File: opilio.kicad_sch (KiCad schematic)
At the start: 92 parts, among them J1 SATA_Power_Connector, J2 USB_C_Receptacle_USB2.0, J3 Conn_01x04_Male, J6 Conn_01x06_Male, Q1 CJ3134KW, Q2 AO3401A, Q3 CJ3134KW, Q4 AO3401A, SW1 Reset, SW2 Boot, U1 EUP3458, U2 STM32F103C8T6, U3 USBLC6-2SC6, Y1 TAXM8M4RFDCET2T, Y2 YST310S 32.768KHz

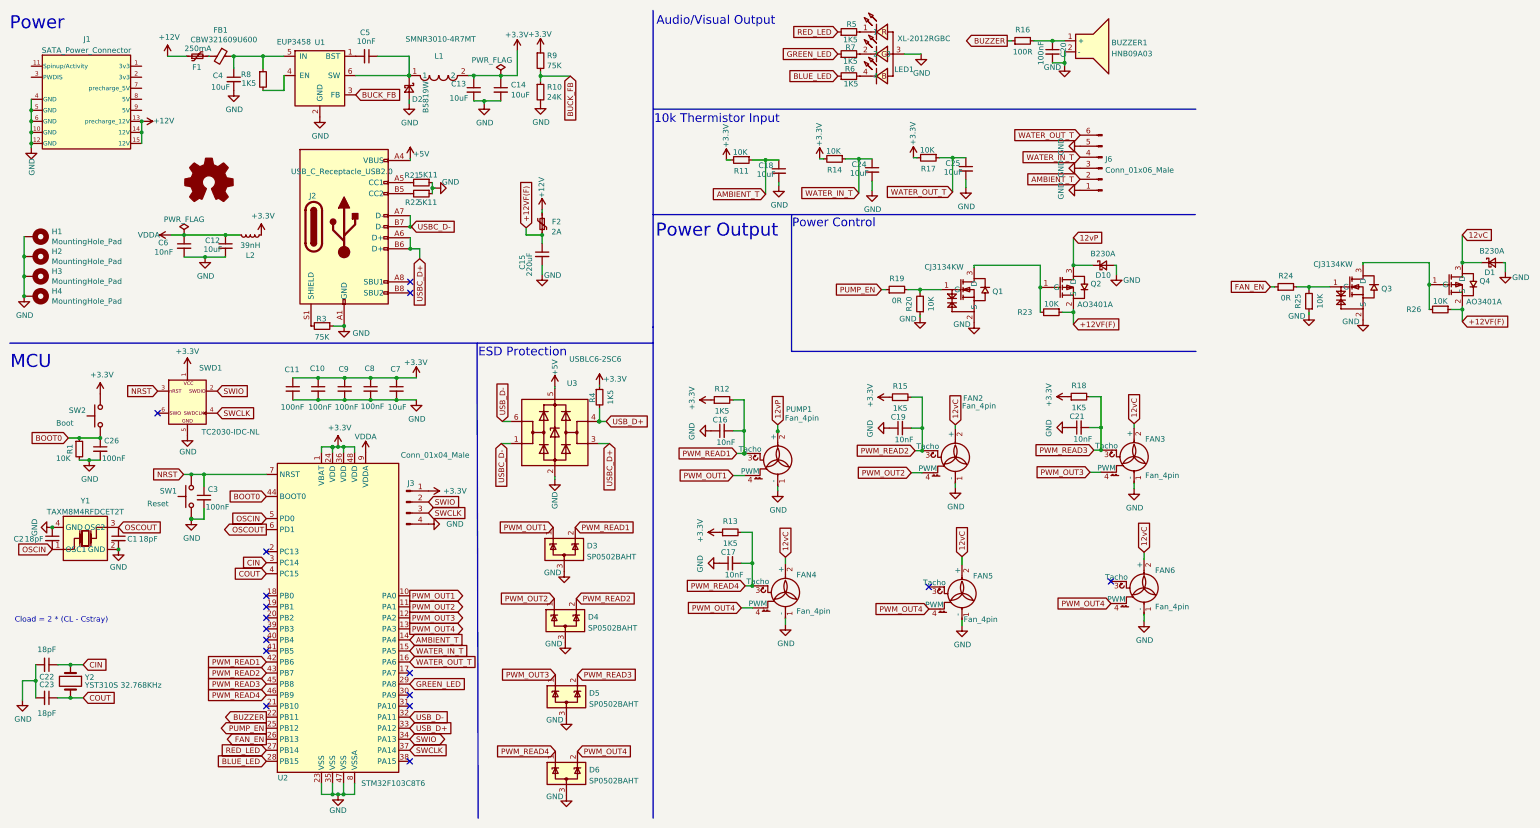
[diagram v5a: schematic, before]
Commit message: split schema, re-route, horizontal fan connectors
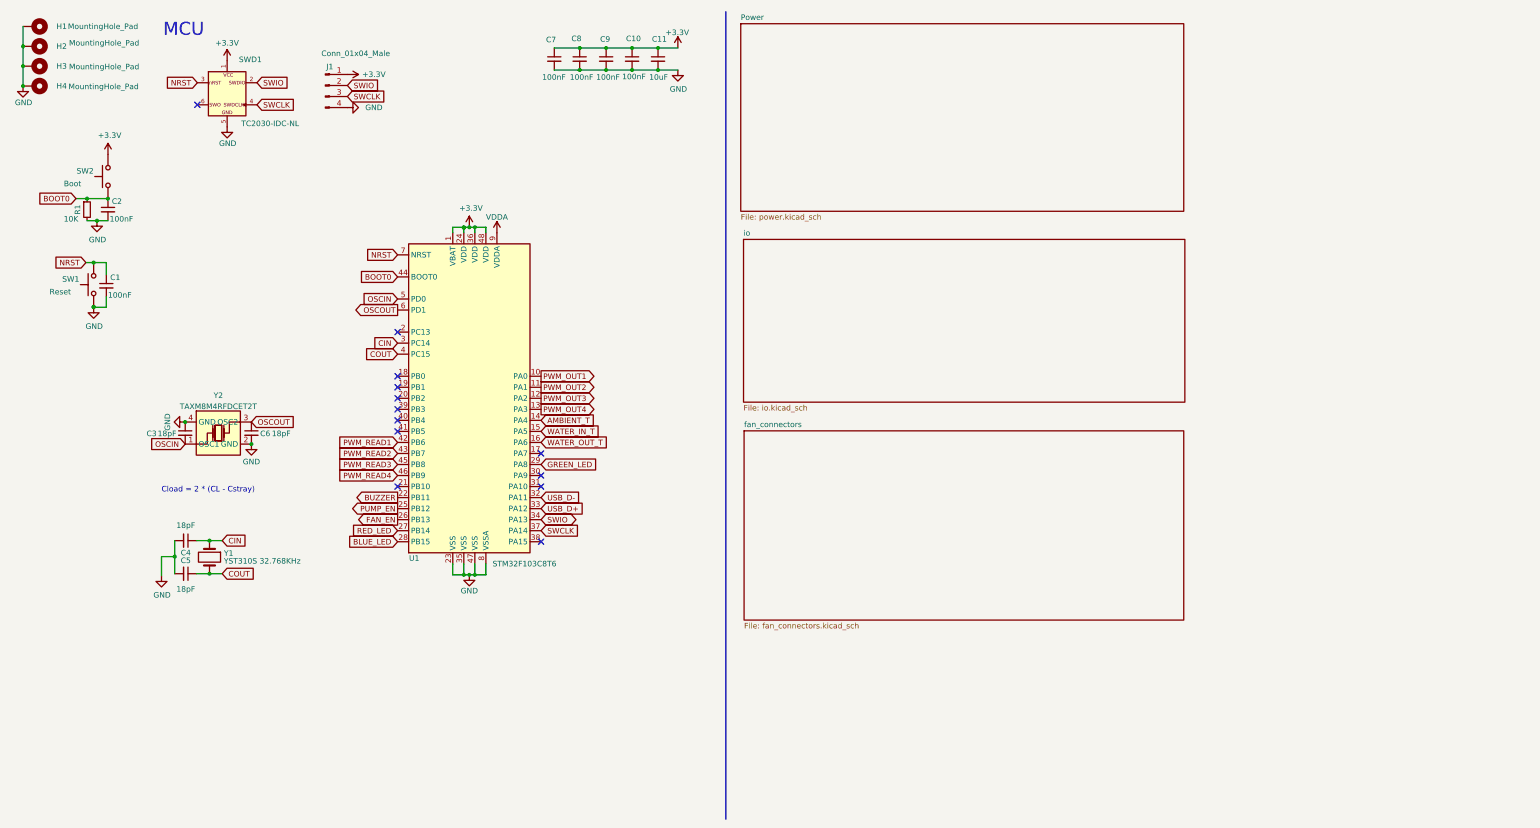
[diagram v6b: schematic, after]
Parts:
- removed BUZZER1: HNB09A03, easyeda2kicad:BUZ-TH_BD9.0-P5.00-D0.6-FD, symbol easyeda:HNB09A03
- removed C12, C13, C14, C18, C24, C25, C4: 10uF, Capacitor_SMD:C_0603_1608Metric, symbol Device:C_Small
- removed C15: 220uF, Capacitor_SMD:CP_Elec_6.3x7.7, symbol Device:C_Small
- removed C16, C17, C19, C21, C5, C6: 10nF, Capacitor_SMD:C_0402_1005Metric, symbol Device:C_Small
- removed C20: 100nF, Capacitor_SMD:C_0402_1005Metric, symbol Device:C_Small
- removed D1, D10: B230A, Diode_SMD:D_SMA, symbol Device:D_Schottky_Small
- removed D2: B5819W, Diode_SMD:D_SOD-123, symbol Device:D_Schottky_Small
- removed D3, D4, D5, D6: SP0502BAHT, Package_TO_SOT_SMD:SOT-23, symbol Power_Protection:SP0502BAHT
- removed F1: 250mA, Fuse:Fuse_1206_3216Metric, symbol Device:Polyfuse_Small
- removed F2: 2A, Fuse:Fuse_1206_3216Metric, symbol Device:Polyfuse_Small
- removed FAN2, FAN3, FAN4, FAN5, FAN6, PUMP1: Fan_4pin, Custom:FanPinHeader_1x04_P2.54mm_Vertical_no_hole, symbol Motor:Fan_4pin
- removed FB1: CBW321609U600, Capacitor_SMD:C_1206_3216Metric, symbol Device:FerriteBead_Small
- removed J1: SATA_Power_Connector, Custom:Sata_Power_Connector_SMD, symbol Custom:SATA_Power_Connector
- removed J2: USB_C_Receptacle_USB2.0, Custom:USB_C_Receptacle_Palconn_UTC16-G_Streached_pads, symbol Connector:USB_C_Receptacle_USB2.0
- removed J6: Conn_01x06_Male, Connector_PinHeader_2.54mm:PinHeader_2x03_P2.54mm_Vertical, symbol Connector:Conn_01x06_Male
- removed L1: SMNR3010-4R7MT, easyeda2kicad:IND-SMD_L3.0-W3.0_SMNR3010, symbol easyeda:SMNR3010-4R7MT
- removed L2: 39nH, Inductor_SMD:L_0805_2012Metric, symbol Device:L_Small
- removed LED1: XL-2012RGBC, easyeda2kicad:LED-SMD_4P-L2.0-W1.3-BR, symbol easyeda:XL-2012RGBC
- removed LOGO1: Logo_Open_Hardware_Small, Symbol:OSHW-Logo2_9.8x8mm_SilkScreen, symbol Graphic:Logo_Open_Hardware_Small
- removed Q1, Q3: CJ3134KW, easyeda2kicad:SC-70-3_L2.1-W1.3-P1.30-LS2.1-BR, symbol easyeda:CJ3134KW
- removed Q2, Q4: AO3401A, easyeda2kicad:SOT-23_L2.9-W1.3-P1.90-LS2.4-BR, symbol easyeda:AO3401A
- removed R10: 24K, Resistor_SMD:R_0402_1005Metric, symbol Device:R_Small
- removed R11, R14, R17, R20, R23, R25, R26: 10K, Resistor_SMD:R_0402_1005Metric, symbol Device:R_Small
- removed R12, R13, R15, R18, R4, R5, R6, R7, R8: 1K5, Resistor_SMD:R_0402_1005Metric, symbol Device:R_Small
- removed R16: 100R, Resistor_SMD:R_0402_1005Metric, symbol Device:R_Small
- removed R19, R24: 0R, Resistor_SMD:R_0402_1005Metric, symbol Device:R_Small
- removed R21, R22: 5K11, Resistor_SMD:R_0402_1005Metric, symbol Device:R_Small
- removed R3, R9: 75K, Resistor_SMD:R_0402_1005Metric, symbol Device:R_Small
- removed U1: EUP3458, Package_TO_SOT_SMD:SOT-23-6, symbol Custom:EUP3458
- removed U3: USBLC6-2SC6, Package_TO_SOT_SMD:SOT-23-6, symbol Power_Protection:USBLC6-2SC6
- renumbered C3 to C1, C8 to C10, C7 to C11, C26 to C2, C2 to C3, C22 to C4, C23 to C5, C1 to C6, C11 to C7, C10 to C8, J3 to J1, U2 to U1, Y2 to Y1, Y1 to Y2
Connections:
- no-connect marks 17 -> 13
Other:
- added sheet Power (power.kicad_sch)
- added sheet fan_connectors (fan_connectors.kicad_sch)
- added sheet io (io.kicad_sch)
- note removed: "10k Thermistor Input"
- note removed: "Audio/Visual Output"
- note removed: "ESD Protection"
- note removed: "Power"
- note removed: "Power Control"
- note removed: "Power Output"
- moved on the sheet: C1, C10, C11, C2, C3, C4, C5, C6, C7, C8, C9, J1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

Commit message: rev-7 ready
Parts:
- removed SW1: Reset, easyeda2kicad:SW-SMD_L3.0-W2.5-P3.40-LS4.0-L, symbol Switch:SW_Push
- removed SW2: Boot, easyeda2kicad:SW-SMD_L3.0-W2.5-P3.40-LS4.0-L, symbol Switch:SW_Push
- added LOGO1: Logo_Open_Hardware_Small, Symbol:OSHW-Logo2_9.8x8mm_SilkScreen, symbol Graphic:Logo_Open_Hardware_Small
- added SW1, SW2: TS-1077S-01726, easyeda2kicad:KEY-SMD_4P-L3.1-W3.1-P2.00_TS-1077S-01726, symbol easyeda:TS-1077S-01726
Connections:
- net +3.3V: now also SW2.1, SW2.2
- net BOOT0: now also SW2.3, SW2.4
- net GND: now also SW1.3, SW1.4, SW1.5, SW2.5
- net NRST: now also SW1.1, SW1.2
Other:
- moved on the sheet: C10, C11, C2, C3, C4, C5, C6, C7, C8, C9, H1, H2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
